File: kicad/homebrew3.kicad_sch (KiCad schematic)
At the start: 36 parts, among them P1 DIP14, P2 DIP14, P3 Conn_02x25_Odd_Even, P4 DIP14, SW1 RESET, SW2 NMI, SW3 9600/4800, SW4 SW_SPDT, SW5 SW_SPDT, SW6 SW_SPDT, U1 Z80CPU, U10 74LS138, U11 74LS139, U12 Z8430, U13 Z8530, U14 Z8420, U15 Z8420, U16 HDSP-2111, U17 20.000MHz, U19 74LS14, U2 MK2716, U20 74LS08, U21 74LS32, U22 MC1489, U23 MC1488, U3 MK2716, U4 TMM2016, U5 TMM2016, U6 74LS245, U7 74LS245, U8 74LS163, U9 74LS04

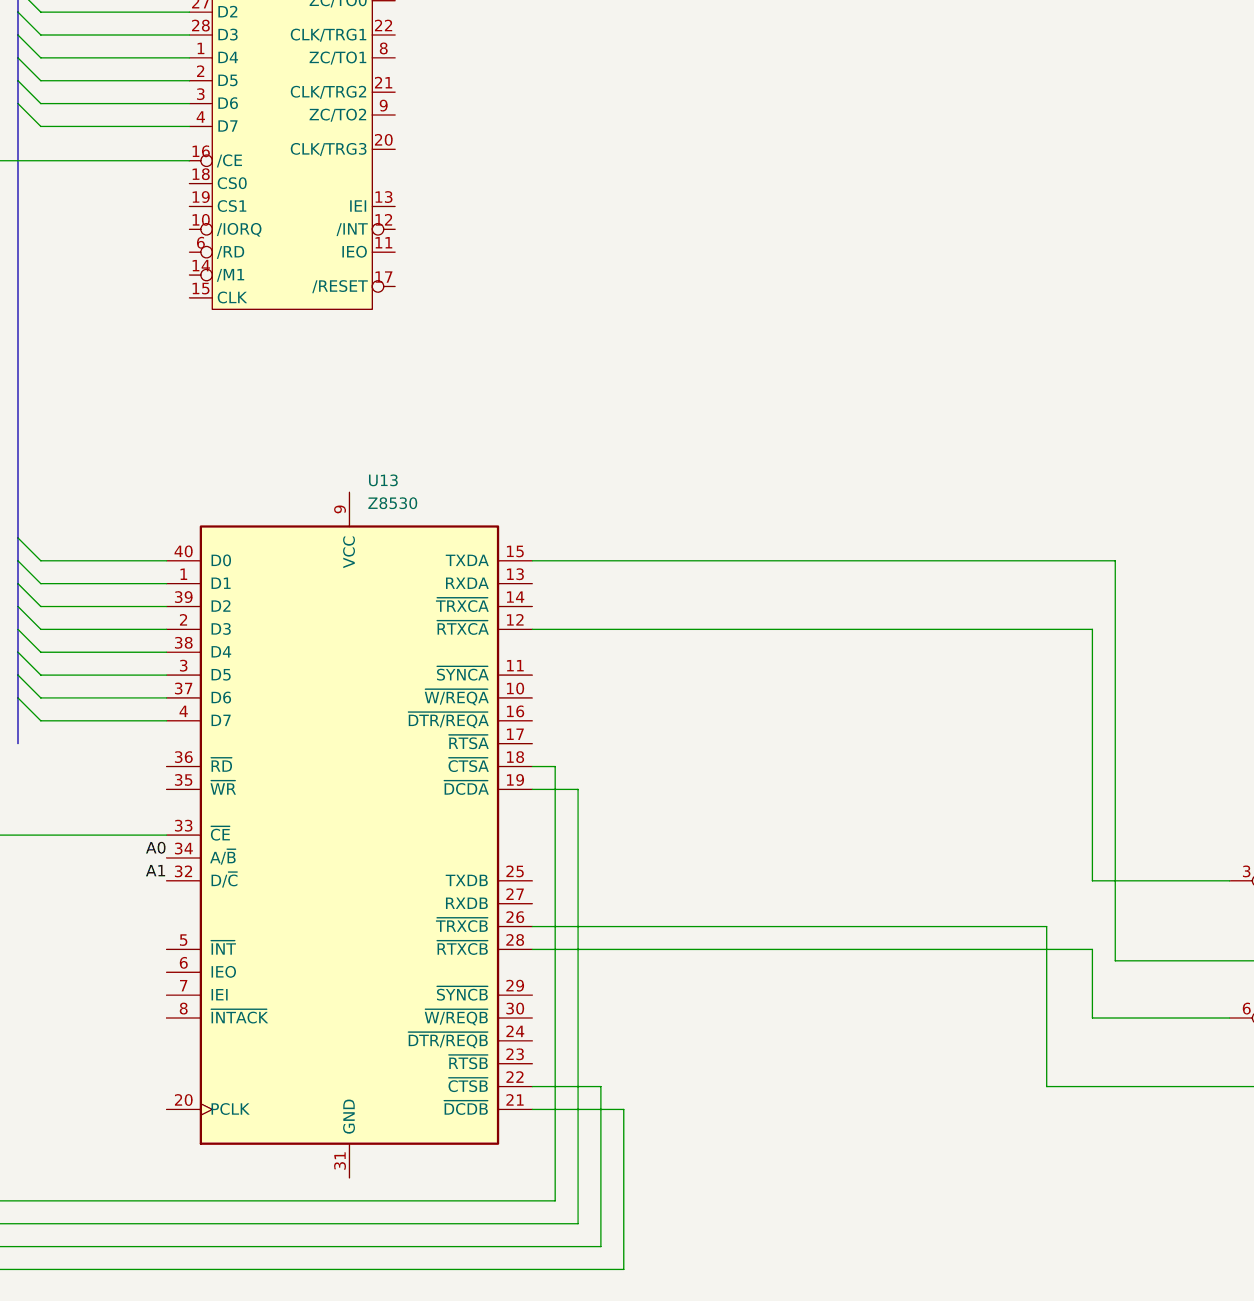
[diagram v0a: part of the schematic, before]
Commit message: Corrections for Z80-SIO/0 in schematic, and I/O decoding signals.
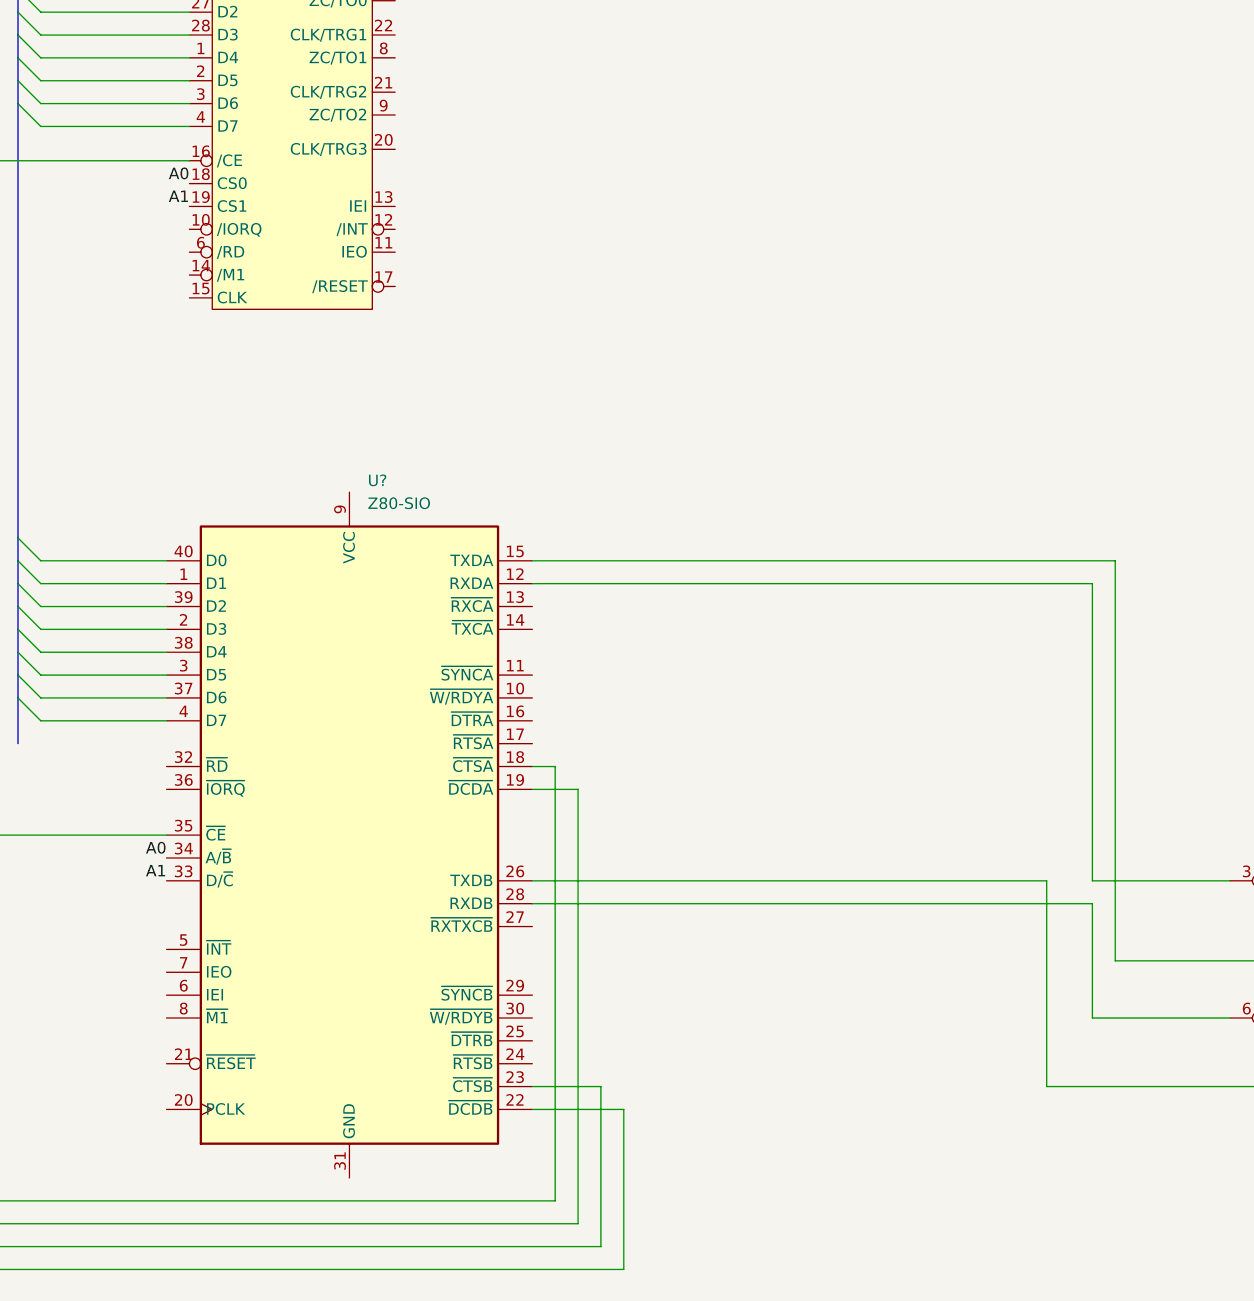
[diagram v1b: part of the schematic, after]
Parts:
- removed U13: Z8530, symbol Interface_UART:Z8530
- added U?: Z80-SIO, symbol homebrew:Z80-SIO
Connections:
- net A0: now also U12.18 (CS0), U?.34 (A/~{B})
- net A1: now also U12.19 (CS1), U?.33 (D/~{C})
- net at U22.3: now also U?.12 (RXDA)
- net at U23.5: now also U?.26 (TXDB)
- net at SW3.2 (B): now also U?.18 (~{CTSA})
- net at U22.6: now also U?.28 (RXDB)
- net at SW6.2 (B): now also U?.22 (~{DCDB})
- net at U23.2: now also U?.15 (TXDA)
- net at SW4.2 (B): now also U?.19 (~{DCDA})
- net at U11.11 (O1): now also U?.35 (~{CE})
- net at SW5.2 (B): now also U?.23 (~{CTSB})
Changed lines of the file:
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@@
     (stroke (width 0) (type default) (color 0 0 0 0))
   )
-  (wire (pts (xy 345.44 454.66) (xy 407.67 454.66))
-    (stroke (width 0) (type default) (color 0 0 0 0))
-  )
   (bus (pts (xy 260.35 96.52) (xy 260.35 99.06))
     (stroke (width 0) (type default) (color 0 0 0 0))
@@
     (stroke (width 0) (type default) (color 0 0 0 0))
   )
-  (wire (pts (xy 407.67 490.22) (xy 407.67 497.84))
+  (wire (pts (xy 407.67 485.14) (xy 407.67 497.84))
     (stroke (width 0) (type default) (color 0 0 0 0))
   )
@@
     (stroke (width 0) (type default) (color 0 0 0 0))
   )
-  (wire (pts (xy 407.67 454.66) (xy 407.67 482.6))
+  (wire (pts (xy 407.67 449.58) (xy 407.67 482.6))
     (stroke (width 0) (type default) (color 0 0 0 0))
   )
@@
     (stroke (width 0) (type default) (color 0 0 0 0))
   )
-  (wire (pts (xy 402.59 487.68) (xy 402.59 505.46))
+  (wire (pts (xy 402.59 482.6) (xy 402.59 505.46))
     (stroke (width 0) (type default) (color 0 0 0 0))
   )
@@
     (stroke (width 0) (type default) (color 0 0 0 0))
   )
-  (wire (pts (xy 345.44 487.68) (xy 402.59 487.68))
-    (stroke (width 0) (type default) (color 0 0 0 0))
-  )
   (bus (pts (xy 337.82 104.14) (xy 337.82 106.68))
     (stroke (width 0) (type default) (color 0 0 0 0))
@@
     (stroke (width 0) (type default) (color 0 0 0 0))
   )
+  (wire (pts (xy 407.67 449.58) (xy 345.44 449.58))
+    (stroke (width 0) (type default) (color 0 0 0 0))
+  )
   (wire (pts (xy 290.83 201.93) (xy 307.34 201.93))
     (stroke (width 0) (type default) (color 0 0 0 0))
@@
     (stroke (width 0) (type default) (color 0 0 0 0))
   )
-  (wire (pts (xy 345.44 490.22) (xy 407.67 490.22))
+  (wire (pts (xy 480.06 123.19) (xy 480.06 130.81))
     (stroke (width 0) (type default) (color 0 0 0 0))
   )
-  (wire (pts (xy 480.06 123.19) (xy 480.06 130.81))
+  (wire (pts (xy 407.67 485.14) (xy 345.44 485.14))
     (stroke (width 0) (type default) (color 0 0 0 0))
   )
@@
     (stroke (width 0) (type default) (color 0 0 0 0))
   )
+  (wire (pts (xy 402.59 482.6) (xy 345.44 482.6))
+    (stroke (width 0) (type default) (color 0 0 0 0))
+  )
   (wire (pts (xy 76.2 148.59) (xy 86.36 148.59))
     (stroke (width 0) (type default) (color 0 0 0 0))
@@
     (effects (font (size 1.27 1.27)) (justify left bottom))
   )
+  (label "A1" (at 307.34 407.67 180)
+    (effects (font (size 1.27 1.27)) (justify right bottom))
+  )
   (label "A6" (at 411.48 102.87 180)
     (effects (font (size 1.27 1.27)) (justify right bottom))
@@
     (effects (font (size 1.27 1.27)) (justify left bottom))
   )
+  (label "A0" (at 307.34 405.13 180)
+    (effects (font (size 1.27 1.27)) (justify right bottom))
+  )
   (label "BA1" (at 441.96 91.44 0)
     (effects (font (size 1.27 1.27)) (justify left bottom))
@@
     (pin "1")
   )
+  (symbol (lib_id "homebrew:Z80-SIO") (at 325.12 474.98 0) (unit 1)
+    (in_bom yes) (on_board yes) (fields_autoplaced)
+    (property "Reference" "U?" (id 0) (at 327.1394 438.15 0)
+      (effects (font (size 1.27 1.27)) (justify left))
+    )
+    (property "Value" "Z80-SIO" (id 1) (at 327.1394 440.69 0)
+      (effects (font (size 1.27 1.27)) (justify left))
+    )
+    (property "Footprint" "" (id 2) (at 325.12 474.345 0)
+      (effects (font (size 1.27 1.27)) hide)
+    )
+    (property "Datasheet" "" (id 3) (at 325.12 474.345 0)
+      (effects (font (size 1.27 1.27)) hide)
+    )
+    (pin "1")
+    (pin "10")
+    (pin "11")
+    (pin "12")
+    (pin "13")
+    (pin "14")
+    (pin "15")
+    (pin "16")
+    (pin "17")
+    (pin "18")
+    (pin "19")
+    (pin "2")
+    (pin "20")
+    (pin "21")
+    (pin "22")
+    (pin "23")
+    (pin "24")
+    (pin "25")
+    (pin "26")
+    (pin "27")
+    (pin "28")
+    (pin "29")
+    (pin "3")
+    (pin "30")
+    (pin "31")
+    (pin "32")
+    (pin "33")
+    (pin "34")
+    (pin "35")
+    (pin "36")
+    (pin "37")
+    (pin "38")
+    (pin "39")
+    (pin "4")
+    (pin "40")
+    (pin "5")
+    (pin "6")
+    (pin "7")
+    (pin "8")
+    (pin "9")
+  )
   (symbol (lib_id "Connector_Generic:Conn_02x07_Counter_Clockwise") (at 469.9 87.63 0) (unit 1)
     (in_bom yes) (on_board yes) (fields_autoplaced)
@@
     (pin "7")
   )
-  (symbol (lib_id "Interface_UART:Z8530") (at 325.12 477.52 0) (unit 1)
-    (in_bom yes) (on_board yes) (fields_autoplaced)
-    (property "Reference" "U13" (id 0) (at 327.1394 438.15 0)
-      (effects (font (size 1.27 1.27)) (justify left))
-    )
-    (property "Value" "Z8530" (id 1) (at 327.1394 440.69 0)
-      (effects (font (size 1.27 1.27)) (justify left))
-    )
-    (property "Footprint" "" (id 2) (at 325.12 477.52 0)
-      (effects (font (size 1.27 1.27)) hide)
-    )
-    (property "Datasheet" "" (id 3) (at 325.12 477.52 0)
-      (effects (font (size 1.27 1.27)) hide)
-    )
-    (pin "1")
-    (pin "10")
-    (pin "11")
-    (pin "12")
-    (pin "13")
-    (pin "14")
-    (pin "15")
-    (pin "16")
-    (pin "17")
-    (pin "18")
-    (pin "19")
-    (pin "2")
-    (pin "20")
-    (pin "21")
-    (pin "22")
-    (pin "23")
-    (pin "24")
-    (pin "25")
-    (pin "26")
-    (pin "27")
-    (pin "28")
-    (pin "29")
-    (pin "3")
-    (pin "30")
-    (pin "31")
-    (pin "32")
-    (pin "33")
-    (pin "34")
-    (pin "35")
-    (pin "36")
-    (pin "37")
-    (pin "38")
-    (pin "39")
-    (pin "4")
-    (pin "40")
-    (pin "5")
-    (pin "6")
-    (pin "7")
-    (pin "8")
-    (pin "9")
-  )
   (symbol (lib_id "Switch:SW_SPDT") (at 227.33 506.73 0) (mirror y) (unit 1)
     (in_bom yes) (on_board yes) (fields_autoplaced)
@@
       (reference "U12") (unit 1) (value "Z8430") (footprint "")
     )
-    (path "/bf372f81-26ba-4fbd-adb4-9c8425014faf"
-      (reference "U13") (unit 1) (value "Z8530") (footprint "")
-    )
     (path "/b6ab959f-2522-4753-ae66-4ecb15674c8b"
       (reference "U14") (unit 1) (value "Z8420") (footprint "Package_DIP:DIP-40_W15.24mm")
@@
       (reference "U23") (unit 2) (value "MC1488") (footprint "")
     )
+    (path "/a5f30593-c9a2-401e-b505-a8d2be1e6629"
+      (reference "U?") (unit 1) (value "Z80-SIO") (footprint "")
+    )
   )

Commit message: Add CTC-SIO connections, misc cleanup.
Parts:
- gave numbers to parts that had none: 1
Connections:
- net GND: now also U2.18 (EP), U3.18 (EP)
- net VCC: now also U16.11 (CLS), U2.21 (VPP), U3.21 (VPP)
- net 1.25MHz: now reaches U8.11 (Q3)
- net 1.25MHz: now also U12.20 (CLK/TRG3), U12.21 (CLK/TRG2), U12.22 (CLK/TRG1), U12.23 (CLK/TRG0)
- net at U12.7 (ZC/TO0): now also U13.13 (~{RXCA}), U13.14 (~{TXCA})
- net at U12.8 (ZC/TO1): now also U13.27 (~{RXTXCB})
- net U16.17: no longer names the net of U16.17 (/CE), U21.6, U21.9
- no-connect marks 6 -> 17
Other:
- moved on the sheet: P4, SW3, SW4, SW5, SW6, U22A, U22B, U23A, U23B

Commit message: Complete more of schematic, incl. assumed PIO connections
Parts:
- P3: value Conn_02x25_Odd_Even -> IDC50-M
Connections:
- net GND: now also P3.1 (Pin_1), P3.13 (Pin_13), P3.14 (Pin_14), P3.2 (Pin_2), P3.25 (Pin_25), P3.26 (Pin_26), P3.37 (Pin_37), P3.38 (Pin_38), P3.49 (Pin_49), P3.50 (Pin_50)
- net VCC: now also U1.24 (~{WAIT}), U1.25 (~{BUSRQ}), U8.9 (~{PE})
- net /RD: now also U16.18 (/RD), U4.20 (OE), U5.20 (OE)
- net /WR: now also U4.21 (WE), U5.21 (WE)
- net at U15.10 (PA4): now also P3.31 (Pin_31)
- net at U15.12 (PA3): now also P3.30 (Pin_30)
- net at U15.13 (PA2): now also P3.29 (Pin_29)
- net at U15.14 (PA1): now also P3.28 (Pin_28)
- net at U15.15 (PA0): now also P3.27 (Pin_27)
- net at U15.27 (PB0): now also P3.39 (Pin_39)
- net at U15.28 (PB1): now also P3.40 (Pin_40)
- net at U15.29 (PB2): now also P3.41 (Pin_41)
- net at U15.30 (PB3): now also P3.42 (Pin_42)
- net at U15.31 (PB4): now also P3.43 (Pin_43)
- net at U15.32 (PB5): now also P3.44 (Pin_44)
- net at U15.33 (PB6): now also P3.45 (Pin_45)
- net at U15.34 (PB7): now also P3.46 (Pin_46)
- net at U15.7 (PA7): now also P3.34 (Pin_34)
- net at U15.8 (PA6): now also P3.33 (Pin_33)
- net at U15.9 (PA5): now also P3.32 (Pin_32)
- net at U14.10 (PA4): now also P3.7 (Pin_7)
- net at U14.12 (PA3): now also P3.6 (Pin_6)
- net at U14.13 (PA2): now also P3.5 (Pin_5)
- net at U14.14 (PA1): now also P3.4 (Pin_4)
- net at U14.15 (PA0): now also P3.3 (Pin_3)
- net at U14.27 (PB0): now also P3.15 (Pin_15)
- net at U14.28 (PB1): now also P3.16 (Pin_16)
- net at U14.29 (PB2): now also P3.17 (Pin_17)
- net at U14.30 (PB3): now also P3.18 (Pin_18)
- net at U14.31 (PB4): now also P3.19 (Pin_19)
- net at U14.32 (PB5): now also P3.20 (Pin_20)
- net at U14.33 (PB6): now also P3.21 (Pin_21)
- net at U14.34 (PB7): now also P3.22 (Pin_22)
- net at U14.7 (PA7): now also P3.10 (Pin_10)
- net at U14.8 (PA6): now also P3.9 (Pin_9)
- net at U14.9 (PA5): now also P3.8 (Pin_8)
- no-connect marks 17 -> 26
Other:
- moved on the sheet: P3

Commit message: Complete more of schematic
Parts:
- added unit 3 of U20
- added unit 1 of U20
- added unit 1 of U9
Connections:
- net ???: now also U20.3, U9.2; no longer P1.14 (Pin_14), P2.13 (Pin_13), U7.1 (A->B)
- net A0: now also U6.2 (A0)
- net A1: now also U6.3 (A1)
- net A2: now also U6.4 (A2)
- net A3: now also U6.5 (A3)
- net A4: now also U6.6 (A4)
- net A5: now also U6.7 (A5)
- net A6: now also U6.8 (A6)
- net A7: now also U6.9 (A7), U9.3
- net /IORQ: now also U20.12, U20.13, U21.1, U21.4
- net /RD: now also U21.10
- net /WR: now also U20.10, U20.9
- net /DSPCE: now reaches U16.17 (/CE), U21.6, U21.9
- net /BIORQ: now reaches U20.11
- net /BIORQ: now also P2.13 (Pin_13)
- net at U21.8: now also U7.1 (A->B)
- new net /BWR: P1.14 (Pin_14), U20.8
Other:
- moved on the sheet: C1, D1, R2, R3, SW1, U19A, U19B, U21B, U21C, U9B

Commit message: Add more connections and cleanup to schematic
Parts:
- added R1: 330, symbol Device:R
- added R4: 5.6K, symbol Device:R
- U8: value 74LS163 -> 74S163
- U9: value 74LS04 -> 74S04
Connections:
- net 2.5MHz: now also U20.2, U9.2, R1.2; no longer U8.12 (Q2)
- net VCC: now also U12.13 (IEI), R1.1, R4.1
- net /NMI: now also SW2.3 (C), U19.10, U19.9; no longer SW2.1 (A), U19.10, U19.9
- net /RESET: now also U20.1
- net at U9.1: now also U8.12 (Q2)
- net at U15.24 (IEI): now also U14.22 (IEO)
- net /XIORD: now reaches U21.8, U7.1 (A->B)
- net at U12.11 (IEO): now also U13.6 (IEI)
- net CTC-CLK: now reaches U12.15 (CLK)
- net CTC-CLK: now also U20.3
- net at U13.7 (IEO): now also U14.24 (IEI)
- removed net ???: U20.3, U9.2
- net /DSPCE renamed /XIORQ
- new net: SW2.1 (A), U19.11, U19.8
- new net /INT: R4.2
- no-connect marks 26 -> 35
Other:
- moved on the sheet: U9A

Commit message: Complete more implied connections on schematic
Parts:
- removed SW1: RESET, symbol Switch:SW_Push
- added SW1: RESET, symbol Switch:SW_Push_SPDT
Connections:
- net 2.5MHz: now also U13.20 (PCLK), U14.25 (CLK), U15.25 (CLK)
- net GND: now also SW1.2 (B); no longer P3.37 (Pin_37)
- net /INT: now also U12.12 (/INT), U13.5 (~{INT}), U14.23 (~{INT}), U15.23 (~{INT})
- net /IORQ: now also U12.10 (/IORQ), U13.36 (~{IORQ}), U14.36 (~{IORQ}), U15.36 (~{IORQ})
- net /RD: now also U12.6 (/RD), U13.32 (~{RD}), U14.35 (~{RD}), U15.35 (~{RD})
- net /RESET: now also P3.37 (Pin_37), U12.17 (/RESET), U13.21 (~{RESET}), U16.1 (/RST)
- net /M1: now reaches U15.37 (~{M1})
- net /M1: now also U12.14 (/M1), U13.8 (~{M1}), U14.37 (~{M1})
- net at R3.2: now also SW1.3 (C)
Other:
- moved on the sheet: SW3, SW4, SW5, SW6

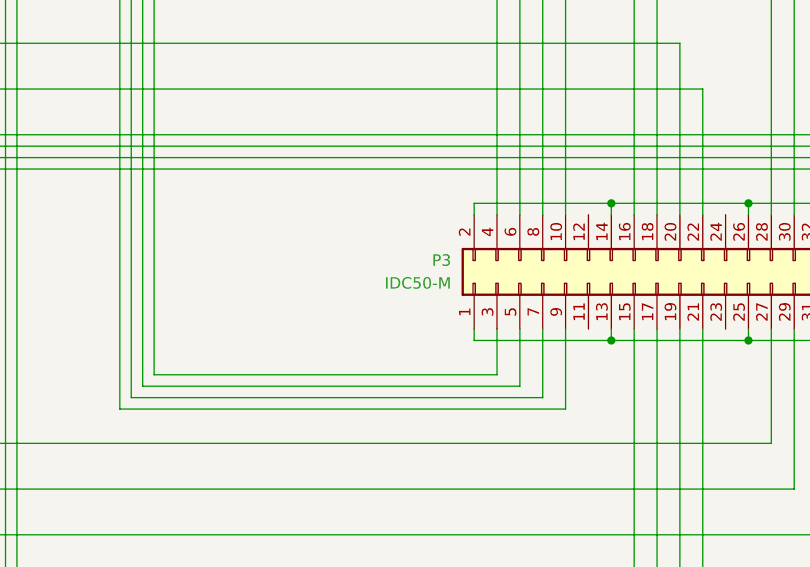
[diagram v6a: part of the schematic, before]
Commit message: Minor cleanup of schematic/BOM
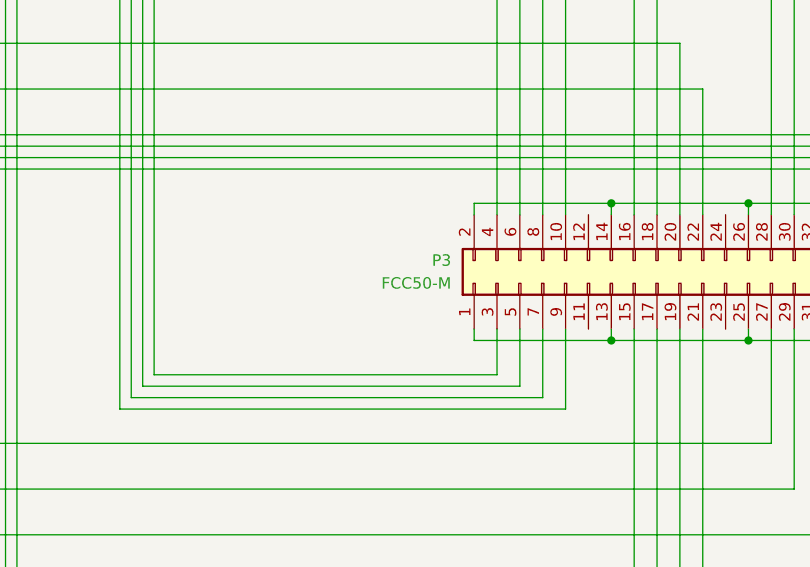
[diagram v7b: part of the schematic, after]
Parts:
- P3: value IDC50-M -> FCC50-M
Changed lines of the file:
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@@
       (effects (font (size 1.27 1.27)) (justify left))
     )
-    (property "Value" "IDC50-M" (id 1) (at 438.15 269.2399 90)
+    (property "Value" "FCC50-M" (id 1) (at 438.15 269.2399 90)
       (effects (font (size 1.27 1.27)) (justify left))
     )
@@
     )
     (path "/e833541e-efe6-4a92-9072-c81cd1e4841c"
-      (reference "P3") (unit 1) (value "IDC50-M") (footprint "")
+      (reference "P3") (unit 1) (value "FCC50-M") (footprint "")
     )
     (path "/4defb757-50aa-4f2a-b979-81b39567a09e"

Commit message: Add examples of wiring to SIO A/B, add system power connections. Cleanup custom symbols.
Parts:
- added J4 (x2): DIP14 Header, symbol Connector_Generic:Conn_02x07_Counter_Clockwise
- added J?: RJ14-F, symbol Connector:4P4C
- added J?: Host, symbol Connector:DB9_Female
- added J?: Console, symbol Connector:DB9_Female
- added P?: RJ14-M, symbol homebrew:RJ14-M
- added U23: MC1488, symbol homebrew:MC1488-PWR
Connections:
- net GND: now also J4.7 (Pin_7), J4.8 (Pin_8), J?.4, P?.4, U23.7 (GND)
- net VCC: now also J4.12 (Pin_12), J4.3 (Pin_3), J?.3, P?.3
- new net: J?.1, J?.4, J?.6 (x2)
- new net: J4.12 (Pin_12), J?.2
- new net: J4.14 (Pin_14), J?.3
- new net: J4.8 (Pin_8), J?.5
- new net: J?.7, J?.8 (x2)
- new net: J4.1 (Pin_1), J?.2
- new net: J4.3 (Pin_3), J?.3
- new net: J4.7 (Pin_7), J?.5
- new net +12V: U23.14 (VCC)
- new net -12V: U23.1 (VEE)
- new net GRN: J4.10 (Pin_10), J4.5 (Pin_5), J?.2, P?.2
- new net Pass-thru?: J4.10 (Pin_10), J4.5 (Pin_5)
- new net YEL: J4.1 (Pin_1), J4.14 (Pin_14), J?.1, P?.1
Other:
- note added: "For USB-RS232 Adapters"
- note added: "Original Equipment Cabling"
- note added: "TODO: check wiring!"
